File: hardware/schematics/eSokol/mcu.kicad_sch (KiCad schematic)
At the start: 10 parts, among them J1 DB25, J2 to HC-05, SW1 SW_LITTLE, U2 YAAJ_BluePill_SWD_Breakout, U3 TP4056, U9 TCRT5000

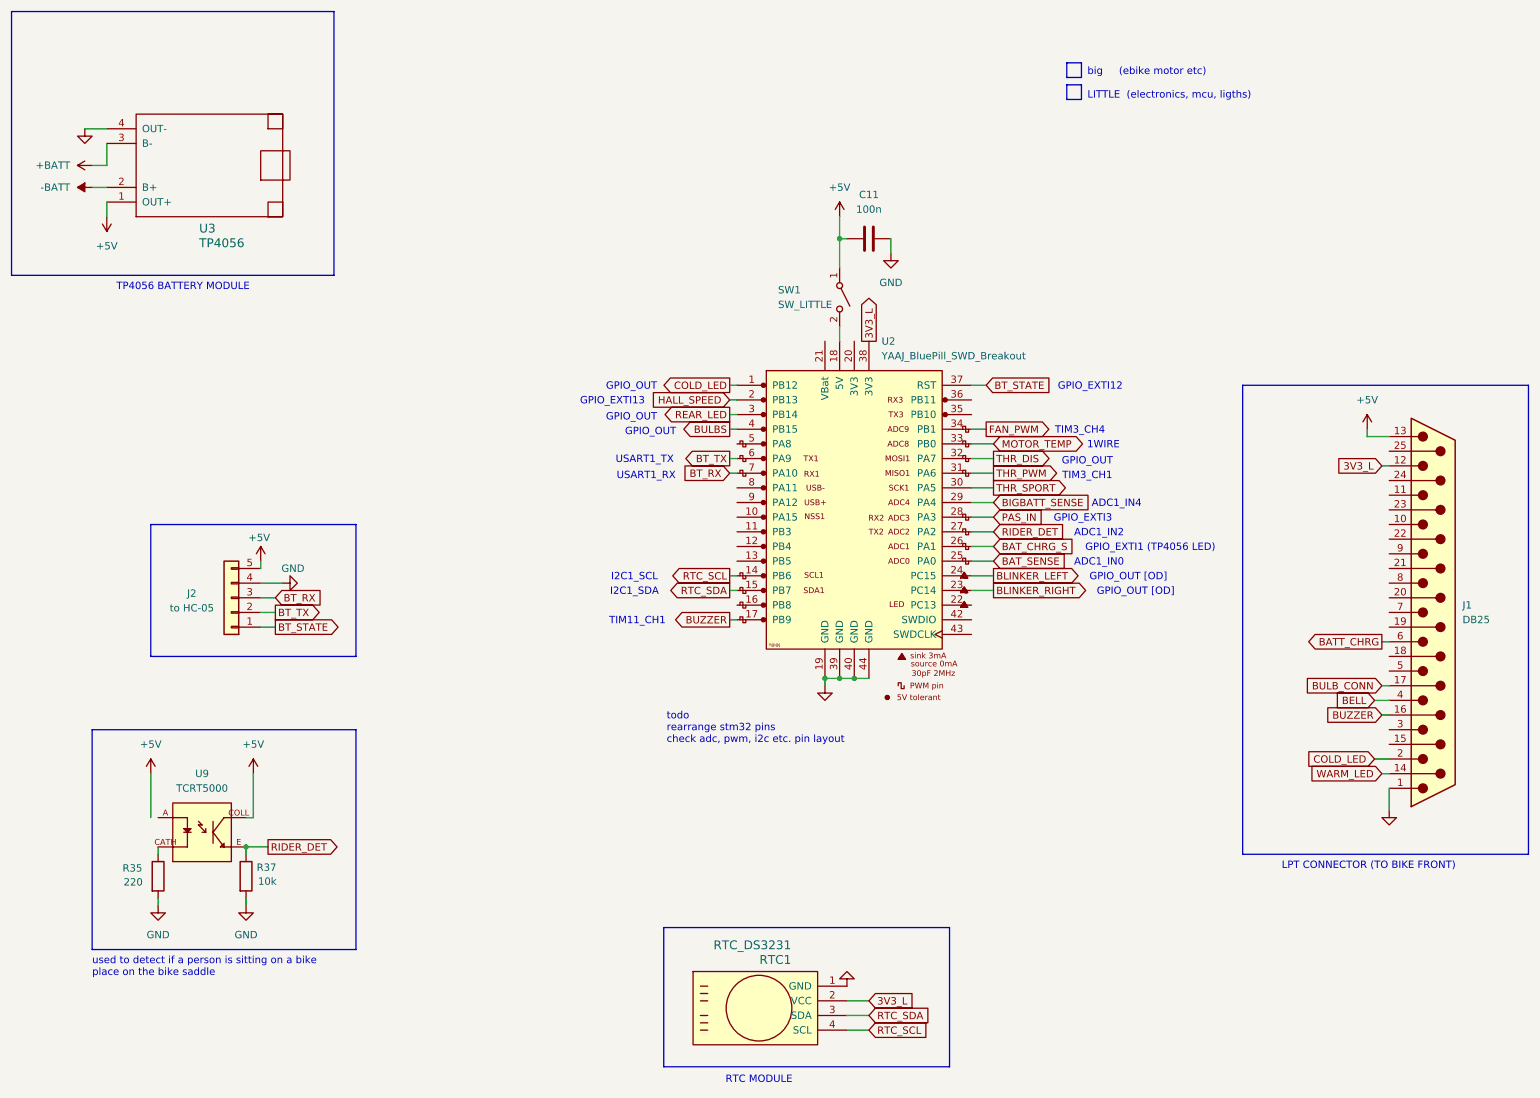
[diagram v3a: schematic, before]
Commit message: hardware/schematics: updated eSokol to reflect new features: ambient light LDR sensor and blinkers Remove old NE555-based blinkers circuit too
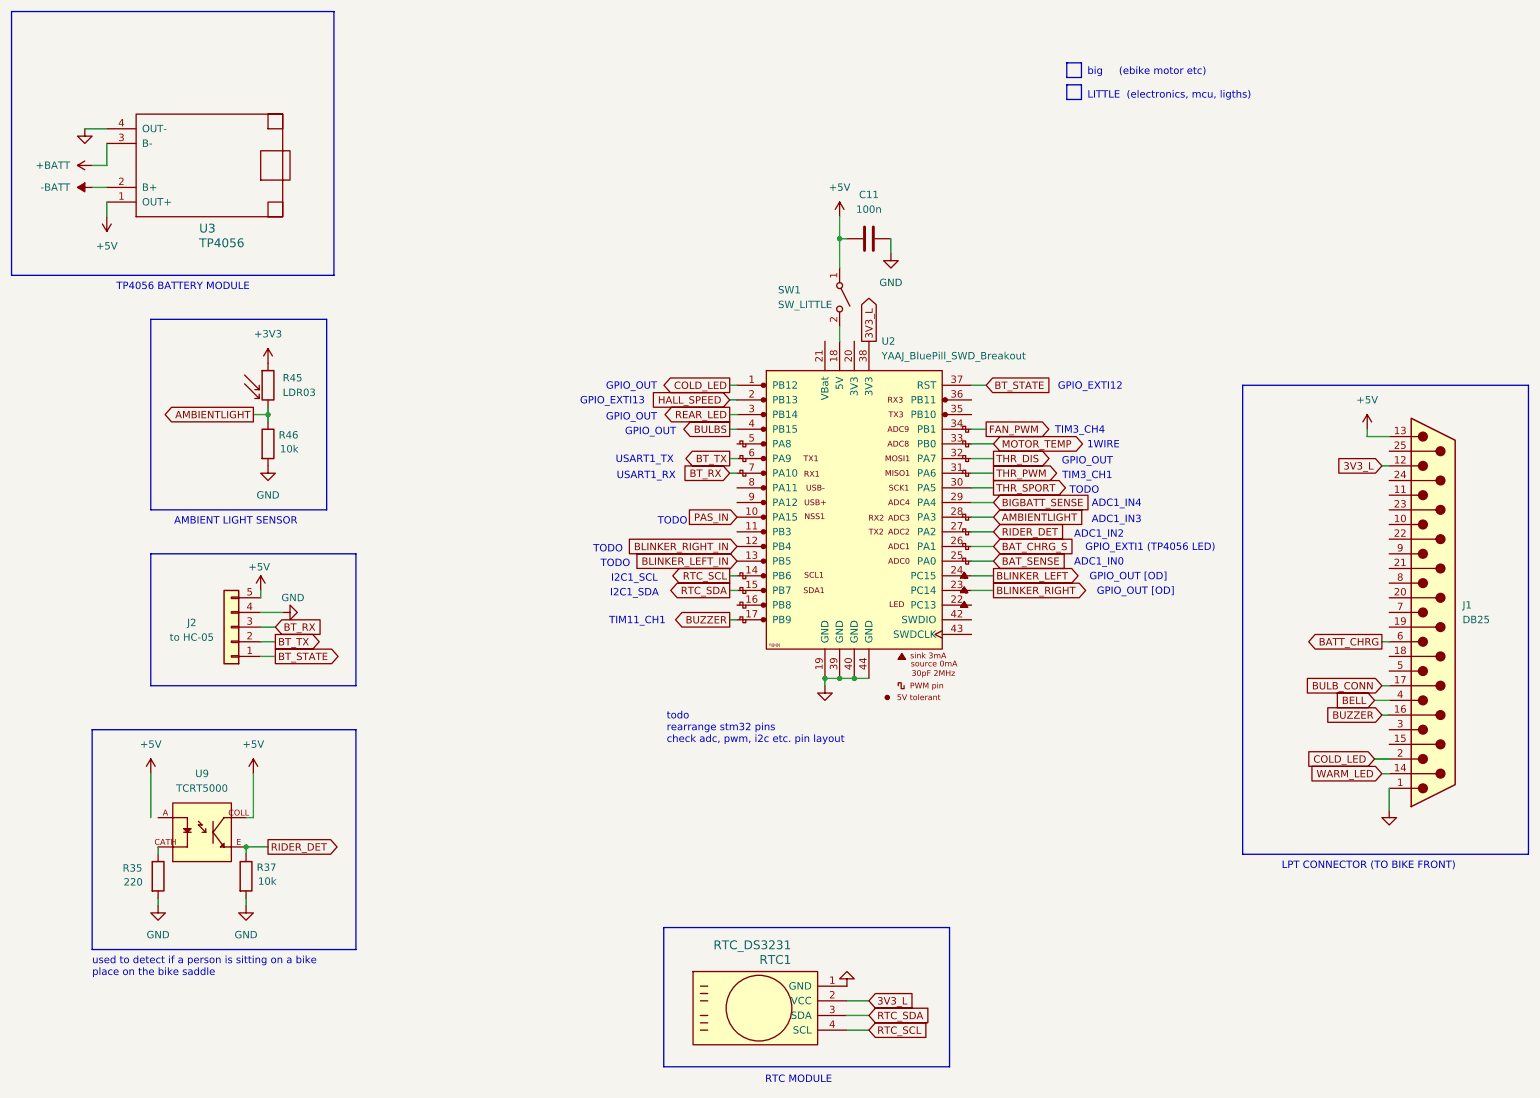
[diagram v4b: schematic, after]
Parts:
- added R45: LDR03, OptoDevice:R_LDR_10x8.5mm_P7.6mm_Vertical, symbol Sensor_Optical:LDR03
- added R46: 10k, symbol Device:R
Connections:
- net GND: now also R46.2
- net PAS_IN: now also U2.10 (PA15); no longer U2.28 (PA3)
- net BLINKER_RIGHT_IN: now reaches U2.12 (PB4)
- net BLINKER_LEFT_IN: now reaches U2.13 (PB5)
- new net +3V3: R45.1
- new net AMBIENTLIGHT: R45.2, R46.1, U2.28 (PA3)
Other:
- note added: "ADC1_IN3"
- note added: "AMBIENT LIGHT SENSOR"
- note added: "TODO"
- note removed: "GPIO_EXTI3"
- moved on the sheet: J2

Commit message: WIP: update some schematics to reflect the newest design changes
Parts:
- added R13: 10k, symbol Device:R
- added R14: R_Shunt, symbol Device:R_Shunt
- added R6: 510k, symbol Device:R
- added U5: LM358, symbol Amplifier_Operational:LM358
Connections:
- net GND: now also R13.1, R14.1
- net THR_DIS renamed THROTTLE_AIN
- net THR_SPORT: no longer names the net of U2.30 (PA5)
- new net: R14.4, U5.3 (+)
- new net: R13.2, R6.1, U5.2 (-)
- new net: R6.2, U5.1
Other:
- note added: "ADCx_INx ??"
- note added: "to lb27 (modded)"
